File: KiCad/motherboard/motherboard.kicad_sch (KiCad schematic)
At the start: 489 parts, among them J1 Barrel_Jack_Switch, J11 Conn_01x06_Pin, J12 Conn_01x06_Pin, J13 Conn_01x04_Pin, J14 Conn_01x04_Pin, J15 Conn_01x04_Pin, J16 Conn_01x05_Socket, J17 DB25_Socket_MountingHoles, J18 Conn_01x09_Pin, J3 Conn_01x04_Pin, J4 Conn_01x05_Pin, Q1 NMOS, Q10 BSS138, Q2 NMOS, Q3 Q_NMOS_Depletion, Q4 Si2371EDS, Q5 BSS138, Q6 BSS138, Q7 BSS138, Q8 BSS138, Q9 BSS138, SW12 SW_Push, SW13 SW_Push, SW14 SW_Push, SW15 SW_Push, SW4 EmergencyStop, SW5 TiltSwitch, SW6 DoorSwitch, SW7 AdditionalSlot, U10 LTV-817S, U11 LTV-817S, U12 LTV-817S, U13 LTV-817S, U14 LTV-817S, U2 TMC2209, U3 TMC2209, U4 ASSR-1218, U5 24LC512, U6 P7805B-1000, U8 LTV-817S, U9 P7803B-1000

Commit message: schematics finished
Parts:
- removed C14, C15, C16, C17: 1u, symbol Device:C
- removed D2: GREEN_LED, symbol Device:LED
- removed D3: SM15T36CA, Diode_SMD:ST_D_SMC, symbol Diode:SM15T36CA
- removed J16: Conn_01x05_Socket, symbol Connector:Conn_01x05_Socket
- removed Q1, Q2: NMOS, symbol Simulation_SPICE:NMOS
- removed Q10, Q7, Q8, Q9: BSS138, Package_TO_SOT_SMD:SOT-23, symbol Transistor_FET:BSS138
- removed Q3: Q_NMOS_Depletion, symbol Device:Q_NMOS_Depletion
- removed Q4: Si2371EDS, Package_TO_SOT_SMD:SOT-23, symbol Transistor_FET:Si2371EDS
- removed R39, R44, R49, R54: 100R, symbol Device:R
- removed R40, R45, R48, R50, R53, R55, R58: 1k, symbol Device:R
- removed R46, R51, R56: 190R, symbol Device:R
- removed R47, R52, R57: 100k, symbol Device:R
- removed TP10, TP11, TP12, TP239, TP240, TP8, TP9: TestPoint, Connector_PinSocket_2.54mm:PinSocket_1x02_P2.54mm_Vertical, symbol Connector:TestPoint
- removed U12, U13, U14, U8: LTV-817S, Package_DIP:SMDIP-4_W9.53mm, symbol Isolator:LTV-817S
- added D2: SZSMF6L24CAT3G, Diode_SMD:D_SOD-123, symbol Device:D_TVS
- added D3: V8PAM103HM3H, Diode_SMD:Vishay_SMPA, symbol Device:D_Schottky
- added J2: Conn_01x02_Socket, TerminalBlock_Phoenix:TerminalBlock_Phoenix_MKDS-1,5-2_1x02_P5.00mm_Horizontal, symbol Connector:Conn_01x02_Socket
- added J5, J6: Conn_01x04_Pin, Connector_PinSocket_2.54mm:PinSocket_1x04_P2.54mm_Vertical, symbol Connector:Conn_01x04_Pin
- added J7, J8: 1761681-9, Connector_PinHeader_2.54mm:PinHeader_2x13_P2.54mm_Vertical, symbol Connector_Generic:Conn_02x13_Odd_Even
- added JP1: SolderJumper_2_Open, Jumper:SolderJumper-2_P1.3mm_Open_RoundedPad1.0x1.5mm, symbol Jumper:SolderJumper_2_Open
- added JP119: SolderJumper_2_Bridged, Resistor_SMD:R_0603_1608Metric, symbol Jumper:SolderJumper_2_Bridged
- added JP120: Jumper_2_Bridged, Connector_PinHeader_2.54mm:PinHeader_1x02_P2.54mm_Vertical, symbol Jumper:Jumper_2_Bridged
- added JP121: SolderJumper_2_Open, Resistor_SMD:R_0603_1608Metric, symbol Jumper:SolderJumper_2_Open
- added JP5: Jumper_2_Open, Connector_PinHeader_2.54mm:PinHeader_1x02_P2.54mm_Vertical, symbol Jumper:Jumper_2_Open
- added Q1, Q11, Q2, Q4: BSS138, Package_TO_SOT_SMD:SOT-23, symbol Transistor_FET:BSS138
- added Q3: SI2369DS-T1-GE3, Package_TO_SOT_SMD:TSOT-23, symbol Simulation_SPICE:PMOS
- added R33, R36: 100k, Resistor_SMD:R_0603_1608Metric, symbol Device:R
- added R34, R35: 1k, Resistor_SMD:R_0603_1608Metric, symbol Device:R
- added U7: ~, Package_SO:TSSOP-14_4.4x5mm_P0.65mm, symbol SymbolLib:LSF0204-Q1
- C1, C6, C7, C8, C9: footprint (none) -> Capacitor_SMD:C_0603_1608Metric
- C2, C3, C4, C5: footprint (none) -> Capacitor_SMD:C_1206_3216Metric
- D1, D10, D11, D4, D5, D6, D7, D8, D9: footprint (none) -> Diode_SMD:D_0603_1608Metric
- F1: value Fuse -> 576-0154007.DRTL; footprint (none) -> Fuse:Fuseholder_Littelfuse_Nano2_154x
- JP2, JP3, JP4: footprint (none) -> Jumper:SolderJumper-2_P1.3mm_Open_RoundedPad1.0x1.5mm
- R1, R14, R15, R16, R17, R18, R19, R2, R20, R21, R22, R23, R24, R25, R26, R27, R28, R29, R3, R30, R4: footprint (none) -> Resistor_SMD:R_0603_1608Metric
- R10: value R -> 27k; footprint (none) -> Resistor_SMD:R_0603_1608Metric
- R11, R12: value R -> 10k; footprint (none) -> Resistor_SMD:R_0603_1608Metric
- R13: value R -> 20k; footprint (none) -> Resistor_SMD:R_0603_1608Metric
- R31, R32: value R -> 4k7; footprint (none) -> Resistor_SMD:R_0603_1608Metric
- R41: value 190R -> 100R; footprint (none) -> Resistor_SMD:R_0603_1608Metric; now not fitted
- R42, R43: footprint (none) -> Resistor_SMD:R_0603_1608Metric; now not fitted
- R5, R8: value R -> 100R; footprint (none) -> Resistor_SMD:R_0603_1608Metric
- R6: value R -> 330R; footprint (none) -> Resistor_SMD:R_0603_1608Metric
- R7: value R -> 100k; footprint (none) -> Resistor_SMD:R_0603_1608Metric; now not fitted
- R9: value 500R -> 150R; footprint (none) -> Resistor_SMD:R_0603_1608Metric
- SW13, SW14, SW15: footprint (none) -> Connector_PinSocket_2.54mm:PinSocket_1x02_P2.54mm_Vertical
- SW4, SW5, SW6, SW7: footprint (none) -> TerminalBlock_Phoenix:TerminalBlock_Phoenix_MKDS-1,5-2_1x02_P5.00mm_Horizontal
- TP7: footprint Connector_PinSocket_2.54mm:PinSocket_1x02_P2.54mm_Vertical -> Connector_PinHeader_2.54mm:PinHeader_1x01_P2.54mm_Vertical
- U6, U9: footprint (none) -> Package_SIP:SIP3_11.6x8.5mm
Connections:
- net GND_SPI_LISTEN is gone; now on net GND: R42.1
- net +24V: now also D3.1 (K), Q3.3 (S)
- net +3V3: now also R43.2, R9.1, R36.1, U7.1 (VREF_A); no longer R8.1
- net +5V: no longer R41.2, U4.4
- net CLK_LISTEN: now also J5.4 (Pin_4), U7.5 (A4)
- net CLK_LISTEN_EXTERNAL: now also J6.4 (Pin_4), J7.4 (Pin_4), J8.4 (Pin_4), U7.10 (B4)
- net GND: now also R7.1, D2.1 (A1), J7.1 (Pin_1), J7.11 (Pin_11), J7.13 (Pin_13), J7.15 (Pin_15), J7.3 (Pin_3), J7.5 (Pin_5), J7.7 (Pin_7), J7.9 (Pin_9), J8.1 (Pin_1), J8.11 (Pin_11), J8.13 (Pin_13), J8.15 (Pin_15), J8.3 (Pin_3), J8.5 (Pin_5), J8.7 (Pin_7), J8.9 (Pin_9), JP1.2 (B), Q1.2 (S), Q11.2 (S), Q2.2 (S), Q4.2 (S), R33.1, U7.7 (GND); no longer U4.2
- net MISO_LISTEN: now also J5.3 (Pin_3), U7.4 (A3)
- net MISO_LISTEN_EXTERNAL: now also J6.3 (Pin_3), J7.6 (Pin_6), J8.6 (Pin_6), U7.11 (B3); no longer TP7.1
- net MOSI_LISTEN: now also J5.2 (Pin_2), U7.3 (A2)
- net MOSI_LISTEN_EXTERNAL: now also J6.2 (Pin_2), J7.8 (Pin_8), J8.8 (Pin_8), U7.12 (B2); no longer R43.2
- net MOT_ENN_DEBOUNCED: now also R41.1, R8.1, JP119.1 (A); no longer R7.1, R9.1
- net NSS_LISTEN: now also J5.1 (Pin_1), U7.2 (A1)
- net NSS_LISTEN_EXTERNAL: now also J6.1 (Pin_1), J7.10 (Pin_10), J8.10 (Pin_10), U7.13 (B1)
- net PDN_UART_MOT1: now also R34.1; no longer U2.3 (PDN/UART), U2.4 (PDN/UART)
- net PDN_UART_MOT2: now also R35.1; no longer U3.3 (PDN/UART), U3.4 (PDN/UART)
- net at R42.2: now also R41.2, Q4.1 (G); no longer R43.1
- net at R1.2, R2.2: now also Q11.1 (G)
- net at R8.2: now also Q1.1 (G), R33.2
- net at D1.1 (K): now also Q2.3 (D)
- net at SW7.1 (A): now also Q11.3 (D)
- net at D4.2 (A), D5.1 (K), F1.2: now also D2.2 (A2), D3.2 (A), Q3.1 (D)
- net at R7.2: now also R5.2, Q2.1 (G)
- net at R11.2, R12.1: now also Q3.2 (G)
- net ISOLATED_ENN_FEEDBACK: no longer names the net of U4.3
- net ISOLATED_ENN_FEEDBACK: now also J2.2 (Pin_2)
- new net: R35.2, U3.3 (PDN/UART), U3.4 (PDN/UART)
- new net: J7.23 (Pin_23), JP120.1 (A)
- new net: JP1.1 (A), R36.2, U7.8 (EN)
- new net: R34.2, U2.3 (PDN/UART), U2.4 (PDN/UART)
- new net: Q1.3 (D), U4.2
- new net: J2.1 (Pin_1), U4.4
- new net: J7.25 (Pin_25), JP5.1 (A)
- new net MOT_ENN: JP119.2 (B), JP121.1 (A)
- new net VCC_SPI: J8.23 (Pin_23), J8.25 (Pin_25), JP120.2 (B), JP5.2 (B), TP7.1, U7.14 (VREF_B)
- new net ~{MOT_ENN_DEBOUNCED}: JP121.2 (B), Q4.3 (D), R43.1
- no-connect marks 6 -> 24
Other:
- note added: "Csatlakozók"
- note added: "ESP32"
- note added: "Logikai szint illesztése"
- note added: "Negált jel lehetősege"
- note added: "Polaritásvédelem"
- note added: "Portok"
- note added: "R7: Amennyiben nem elegendő a vele párhuzamos út a spontán töltések elvezetésére"
- note added: "SPI IN"
- note added: "SPI OUT"
- note added: "Tápellátás"
- note added: "Túlfeszültségvédelem"
- note removed: "100R miért? Csak, h ne közvetlenül menjen?"
- note removed: "ESD"
- note removed: "Ez csak placeholder, meg kell beszélni a típusát még"
- note removed: "Ez nem tudom, jó választás-e. Azért ez van itt, mert ez már bennt volt a könyvtárnam, kétiránú és VRM = 30.8V"
- note removed: "Ez így miért nem jó, hogy nem 5V és 3v3 zener, hanem simán a 3v3-at kapcsolom"
- note removed: "Polarity indication"
- note removed: "Polarity indication?"
- note removed: "Pull downt azért raktam, mert le van választva -> nincs aktívan hajtva az alacsony szint Nem terheli ezn agyon a lehallgatottat? Milyen csati kellene?"
- note removed: "todo: footprintek kapcsolóknak csati, MOSFET-eket kell választani"
- moved on the sheet: C1, C18, C19, C20, C21, C8, C9, D1, D4, D5, F1, J1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

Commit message: PCB designs started
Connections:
- net BTN_FIX_AX: now also J18.3 (Pin_3), JP41.2 (B), TP96.1; no longer J18.2 (Pin_2), JP40.2 (B), TP95.1
- net BTN_MEMSLOT: now also J18.2 (Pin_2), JP40.2 (B), TP95.1; no longer J18.4 (Pin_4), JP42.2 (B), TP97.1
- net BTN_SET: now also J18.4 (Pin_4), JP42.2 (B), TP97.1; no longer J18.6 (Pin_6), JP44.2 (B), TP99.1
- net BTN_TRACKED_AX: now also J18.6 (Pin_6), JP44.2 (B), TP99.1; no longer J18.3 (Pin_3), JP41.2 (B), TP96.1

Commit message: main board pcb design started
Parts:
- TP100, TP101, TP102, TP103, TP104, TP105, TP106, TP107, TP108, TP109, TP110, TP111, TP112, TP113, TP114, TP115, TP116, TP117, TP118, TP119, TP120, TP121, TP122, TP123, TP124, TP125, TP126, TP127, TP128, TP129, TP13, TP130, TP131, TP132, TP133, TP134, TP135, TP136, TP137, TP138, TP139, TP14, TP140, TP141, TP142, TP143, TP144, TP145, TP146, TP147, TP148, TP149, TP15, TP150, TP151, TP152, TP153, TP154, TP155, TP156, TP157, TP158, TP159, TP16, TP160, TP161, TP162, TP163, TP164, TP165, TP166, TP167, TP168, TP169, TP17, TP170, TP171, TP172, TP173, TP174, TP175, TP176, TP177, TP178, TP179, TP18, TP180, TP181, TP182, TP183, TP184, TP185, TP186, TP187, TP188, TP189, TP19, TP190, TP191, TP192, TP193, TP194, TP195, TP196, TP197, TP198, TP199, TP20, TP200, TP201, TP202, TP203, TP204, TP205, TP206, TP207, TP208, TP209, TP21, TP210, TP211, TP212, TP213, TP214, TP215, TP216, TP217, TP218, TP219, TP22, TP220, TP221, TP222, TP223, TP224, TP225, TP226, TP227, TP228, TP229, TP23, TP230, TP231, TP232, TP233, TP234, TP235, TP236, TP237, TP238, TP24, TP241, TP242, TP25, TP26, TP27, TP28, TP29, TP30, TP31, TP32, TP33, TP34, TP35, TP36, TP37, TP38, TP39, TP40, TP41, TP42, TP43, TP44, TP45, TP46, TP47, TP48, TP49, TP50, TP51, TP52, TP53, TP54, TP55, TP56, TP57, TP58, TP59, TP60, TP61, TP62, TP63, TP64, TP65, TP66, TP67, TP68, TP69, TP70, TP71, TP72, TP73, TP74, TP75, TP76, TP77, TP78, TP79, TP80, TP81, TP82, TP83, TP84, TP85, TP86, TP87, TP88, TP89, TP90, TP91, TP92, TP93, TP94, TP95, TP96, TP97, TP98, TP99: footprint Connector_PinSocket_2.54mm:PinSocket_1x02_P2.54mm_Vertical -> Connector_PinSocket_2.54mm:PinSocket_1x01_P2.54mm_Vertical
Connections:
- net MOT_ENN: now also R5.1
- net MOT_ENN_DEBOUNCED: no longer R5.1
- net at U4.3: now also J2.1 (Pin_1); no longer J2.2 (Pin_2)
- net at U4.4: now also J2.2 (Pin_2); no longer J2.1 (Pin_1)
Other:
- note added: "Level shifter kikapcsolható J1 zárásával"
- moved on the sheet: J2

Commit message: main board pcb continued
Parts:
- added JP122, JP123, JP124, JP125, JP126, JP127, JP128, JP129, JP130, JP131, JP132, JP133, JP134, JP135, JP136, JP137, JP138, JP139, JP140, JP141, JP142, JP67, JP68, JP69, JP70, JP71, JP72: SolderJumper_2_Open, Resistor_SMD:R_0603_1608Metric_Pad0.98x0.95mm_HandSolder, symbol Jumper:SolderJumper_2_Open
- added TP131, TP132, TP133, TP134, TP135, TP136, TP185, TP186, TP187, TP188, TP189, TP190, TP240, TP241, TP242, TP243, TP244, TP245, TP246, TP247, TP248, TP249, TP250, TP251, TP252, TP253, TP254, TP255, TP256, TP257, TP258, TP259, TP260, TP262, TP263, TP264, TP265, TP266, TP267, TP268, TP269, TP270, TP271, TP272, TP273, TP274, TP275, TP276, TP277, TP278, TP279, TP280, TP281, TP282: TestPoint_Small, Connector_PinSocket_2.54mm:PinSocket_1x01_P2.54mm_Vertical, symbol Connector:TestPoint_Small
- renumbered C4 to C1, C20 to C10, C9 to C11, C7 to C12, C21 to C13, C1 to C3, C5 to C4, C3 to C5, C18 to C6, C6 to C7, C19 to C8, C8 to C9, D2 to D1, D11 to D10, D10 to D11, D4 to D2, D5 to D3, D3 to D4, D8 to D5, D7 to D6, D6 to D7, D1 to D8, J11 to J1, J15 to J10, J17 to J11, J5 to J12, J7 to J13, J6 to J14, J8 to J15, J1 to J2, J12 to J5, J13 to J6, J18 to J7, J2 to J8, J14 to J9, JP121 to JP1, JP13 to JP10, JP97 to JP100, JP98 to JP101, JP99 to JP102, JP100 to JP103, JP101 to JP104, JP54 to JP105, JP55 to JP106, JP56 to JP107, JP57 to JP108, JP58 to JP109, JP14 to JP11, JP59 to JP110, JP60 to JP111, JP61 to JP112, JP62 to JP113, JP63 to JP114, JP64 to JP115, JP65 to JP116, JP66 to JP117, JP67 to JP118, JP68 to JP119, JP15 to JP12, JP69 to JP120, JP118 to JP121, JP16 to JP13, JP17 to JP14, JP3 to JP143, JP5 to JP144, JP4 to JP145, JP120 to JP146, JP2 to JP147, JP1 to JP148, JP18 to JP15, JP19 to JP16, JP20 to JP17, JP21 to JP18, JP70 to JP19, JP119 to JP2, JP71 to JP20, JP72 to JP21, JP73 to JP22, JP74 to JP23, JP75 to JP24, JP76 to JP25, JP77 to JP26, JP78 to JP27, JP79 to JP28, JP80 to JP29, JP6 to JP3, JP81 to JP30, JP82 to JP31, JP83 to JP32, JP84 to JP33, JP85 to JP34, JP38 to JP35, JP39 to JP36, JP40 to JP37, JP41 to JP38, JP42 to JP39, JP7 to JP4, JP43 to JP40, JP44 to JP41, JP45 to JP42, JP46 to JP43, JP47 to JP44, JP48 to JP45, JP49 to JP46, JP50 to JP47, JP51 to JP48, JP52 to JP49, JP8 to JP5, JP53 to JP50, JP102 to JP51, JP103 to JP52, JP104 to JP53, JP105 to JP54, JP106 to JP55, JP107 to JP56, JP108 to JP57, JP109 to JP58, JP110 to JP59, JP9 to JP6, JP111 to JP60, JP112 to JP61, JP113 to JP62, JP114 to JP63, JP115 to JP64, JP116 to JP65, JP117 to JP66, JP10 to JP7, JP22 to JP73, JP23 to JP74, JP24 to JP75, JP25 to JP76, JP26 to JP77, JP27 to JP78, JP28 to JP79, JP11 to JP8, JP29 to JP80, JP30 to JP81, JP31 to JP82, JP32 to JP83, JP33 to JP84, JP34 to JP85, JP35 to JP86, JP36 to JP87, JP37 to JP88, JP86 to JP89, JP12 to JP9, JP87 to JP90, JP88 to JP91, JP89 to JP92, JP90 to JP93, JP91 to JP94, JP92 to JP95, JP93 to JP96, JP94 to JP97, JP95 to JP98, JP96 to JP99, Q11 to Q1, Q4 to Q2, Q1 to Q4, Q2 to Q5, Q5 to Q6, Q6 to Q7, R15 to R10, R14 to R11, R11 to R12, R8 to R14, R33 to R15, R5 to R16, R9 to R17, R7 to R18, R6 to R19, R34 to R20, R35 to R21, R31 to R22, R32 to R23, R16 to R24, R59 to R25, R60 to R26, R61 to R27, R62 to R28, R17 to R29, R41 to R3, R29 to R30, R18 to R31, R25 to R32, R19 to R33, R30 to R34, R24 to R35, R28 to R36, R63 to R37, R64 to R38, R22 to R39, R3 to R4, R23 to R40, R21 to R41, R26 to R42, R20 to R43, R27 to R44, R65 to R45, R66 to R46, R36 to R47, R42 to R5, R4 to R6, R43 to R7, R10 to R8, R12 to R9, SW4 to SW1, SW5 to SW2, SW6 to SW3, SW7 to SW4, SW12 to SW5, SW13 to SW6, SW14 to SW7, SW15 to SW8, TP15 to TP1, TP31 to TP10, TP96 to TP100, TP97 to TP101, TP98 to TP102, TP99 to TP103, TP100 to TP104, TP101 to TP105, TP102 to TP106, TP103 to TP107, TP104 to TP108, TP105 to TP109, TP33 to TP11, TP106 to TP110, TP107 to TP111, TP108 to TP112, TP221 to TP113, TP222 to TP114, TP223 to TP115, TP224 to TP116, TP225 to TP117, TP226 to TP118, TP227 to TP119, TP35 to TP12, TP228 to TP120, TP229 to TP121, TP230 to TP122, TP231 to TP123, TP232 to TP124, TP233 to TP125, TP234 to TP126, TP235 to TP127, TP236 to TP128, TP241 to TP129, TP37 to TP13, TP242 to TP130, TP45 to TP137, TP46 to TP138, TP47 to TP139, TP39 to TP14, TP48 to TP140, TP49 to TP141, TP50 to TP142, TP51 to TP143, TP52 to TP144, TP53 to TP145, TP54 to TP146, TP55 to TP147, TP56 to TP148, TP57 to TP149, TP41 to TP15, TP58 to TP150, TP59 to TP151, TP60 to TP152, TP173 to TP153, TP174 to TP154, TP175 to TP155, TP176 to TP156, TP177 to TP157, TP178 to TP158, TP179 to TP159, TP43 to TP16, TP180 to TP160, TP181 to TP161, TP182 to TP162, TP183 to TP163, TP184 to TP164, TP185 to TP165, TP186 to TP166, TP187 to TP167, TP188 to TP168, TP109 to TP169, TP141 to TP17, TP110 to TP170, TP111 to TP171, TP112 to TP172, TP113 to TP173, TP114 to TP174, TP115 to TP175, TP116 to TP176, TP117 to TP177, TP118 to TP178, TP119 to TP179, TP142 to TP18, TP120 to TP180, TP121 to TP181, TP122 to TP182, TP123 to TP183, TP124 to TP184, TP143 to TP19, TP61 to TP191, TP62 to TP192, TP63 to TP193, TP64 to TP194, TP65 to TP195, TP66 to TP196, TP67 to TP197, TP68 to TP198, TP69 to TP199, TP14 to TP2, TP144 to TP20, TP70 to TP200, TP71 to TP201, TP72 to TP202, TP73 to TP203, TP74 to TP204, TP75 to TP205, TP76 to TP206, TP189 to TP207, TP190 to TP208, TP191 to TP209, TP145 to TP21, TP192 to TP210, TP193 to TP211, TP194 to TP212, TP195 to TP213, TP196 to TP214, TP197 to TP215, TP198 to TP216, TP199 to TP217, TP200 to TP218, TP201 to TP219, TP146 to TP22, TP202 to TP220, TP203 to TP221, TP204 to TP222, TP125 to TP223, TP126 to TP224, TP127 to TP225, TP128 to TP226, TP129 to TP227, TP130 to TP228, TP131 to TP229, TP147 to TP23, TP132 to TP230, TP133 to TP231, TP134 to TP232, TP135 to TP233, TP136 to TP234, TP137 to TP235, TP138 to TP236, TP139 to TP237, TP140 to TP238, TP237 to TP239, TP148 to TP24, TP149 to TP25, TP150 to TP26, TP238 to TP261, TP151 to TP27, TP152 to TP28, TP6 to TP283, TP5 to TP284, TP4 to TP285, TP1 to TP286, TP7 to TP287, TP3 to TP288, TP2 to TP289, TP153 to TP29, TP17 to TP3, TP154 to TP30, TP155 to TP31, TP156 to TP32, TP77 to TP33, TP78 to TP34, TP79 to TP35, TP80 to TP36, TP81 to TP37, TP82 to TP38, TP83 to TP39, TP19 to TP4, TP84 to TP40, TP85 to TP41, TP86 to TP42, TP87 to TP43, TP88 to TP44, TP89 to TP45, TP90 to TP46, TP91 to TP47, TP92 to TP48, TP205 to TP49, TP21 to TP5, TP206 to TP50, TP207 to TP51, TP208 to TP52, TP209 to TP53, TP210 to TP54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
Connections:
- net GND: now also JP131.2 (B), JP132.2 (B), JP133.2 (B), JP134.2 (B), JP135.2 (B), JP136.2 (B), JP137.2 (B), JP138.2 (B), JP139.2 (B), JP140.2 (B), JP141.2 (B), JP142.2 (B), TP271.1, TP272.1, TP273.1, TP274.1, TP275.1, TP276.1, TP277.1, TP278.1, TP279.1, TP280.1, TP281.1, TP282.1; no longer U3.11-19 (GND), U3.11-20 (GND), U3.11-22 (GND), U3.11-49 (GND), U3.11-60 (GND), U3.11-8 (GND), U3.12-20 (GND), U3.12-32 (AGND), U3.12-39 (GND), U3.12-54 (GND), U3.12-63 (GND), U3.12-9 (GND)
- net at U3.11-12 (IOREF): now also JP126.1 (A), TP244.1
- net at U3.11-14 (RESET): now also JP130.1 (A), TP248.1
- net at U3.11-16 (3V3): now also JP125.1 (A), TP243.1
- net at U3.11-18 (5V): now also JP124.1 (A), TP242.1
- net at U3.11-24 (VIN): now also JP123.1 (A), TP241.1
- net at U3.11-33 (VBAT): now also JP122.1 (A), TP240.1
- net at U3.11-5 (VDD): now also JP127.1 (A), TP245.1
- net at U3.12-7 (AVDD): now also JP129.1 (A), TP247.1
- net at U3.12-8 (U5V): now also JP128.1 (A), TP246.1
- net at U3.11-10 (NC): now also JP72.1 (A), TP136.1
- net at U3.11-26 (NC): now also JP71.1 (A), TP135.1
- net at U3.11-29 (PH0): now also JP67.1 (A), TP131.1
- net at U3.11-31 (PH1): now also JP68.1 (A), TP132.1
- net at U3.11-67 (NC): now also JP70.1 (A), TP134.1
- net at U3.11-7 (BOOT0): now also JP69.1 (A), TP133.1
- new net: JP124.2 (B), TP264.1
- new net: JP132.1 (A), TP250.1, U3.11-19 (GND)
- new net: JP133.1 (A), TP251.1, U3.11-20 (GND)
- new net: JP134.1 (A), TP252.1, U3.11-22 (GND)
- new net: JP139.1 (A), TP257.1, U3.11-49 (GND)
- new net: JP141.1 (A), TP259.1, U3.11-60 (GND)
- new net: JP140.1 (A), TP258.1, U3.11-8 (GND)
- new net: JP135.1 (A), TP253.1, U3.12-20 (GND)
- new net: JP131.1 (A), TP249.1, U3.12-32 (AGND)
- new net: JP136.1 (A), TP254.1, U3.12-39 (GND)
- new net: JP137.1 (A), TP255.1, U3.12-54 (GND)
- new net: JP138.1 (A), TP256.1, U3.12-63 (GND)
- new net: JP142.1 (A), TP260.1, U3.12-9 (GND)
- new net: JP72.2 (B), TP190.1
- new net: JP68.2 (B), TP186.1
- new net: JP67.2 (B), TP185.1
- new net: JP69.2 (B), TP187.1
- new net: JP130.2 (B), TP270.1
- new net: JP122.2 (B), TP262.1
- new net: JP127.2 (B), TP267.1
- new net: JP126.2 (B), TP266.1
- new net: JP128.2 (B), TP268.1
- new net: JP70.2 (B), TP188.1
- new net: JP123.2 (B), TP263.1
- new net: JP71.2 (B), TP189.1
- new net: JP129.2 (B), TP269.1
- new net: JP125.2 (B), TP265.1
- no-connect marks 24 -> 33

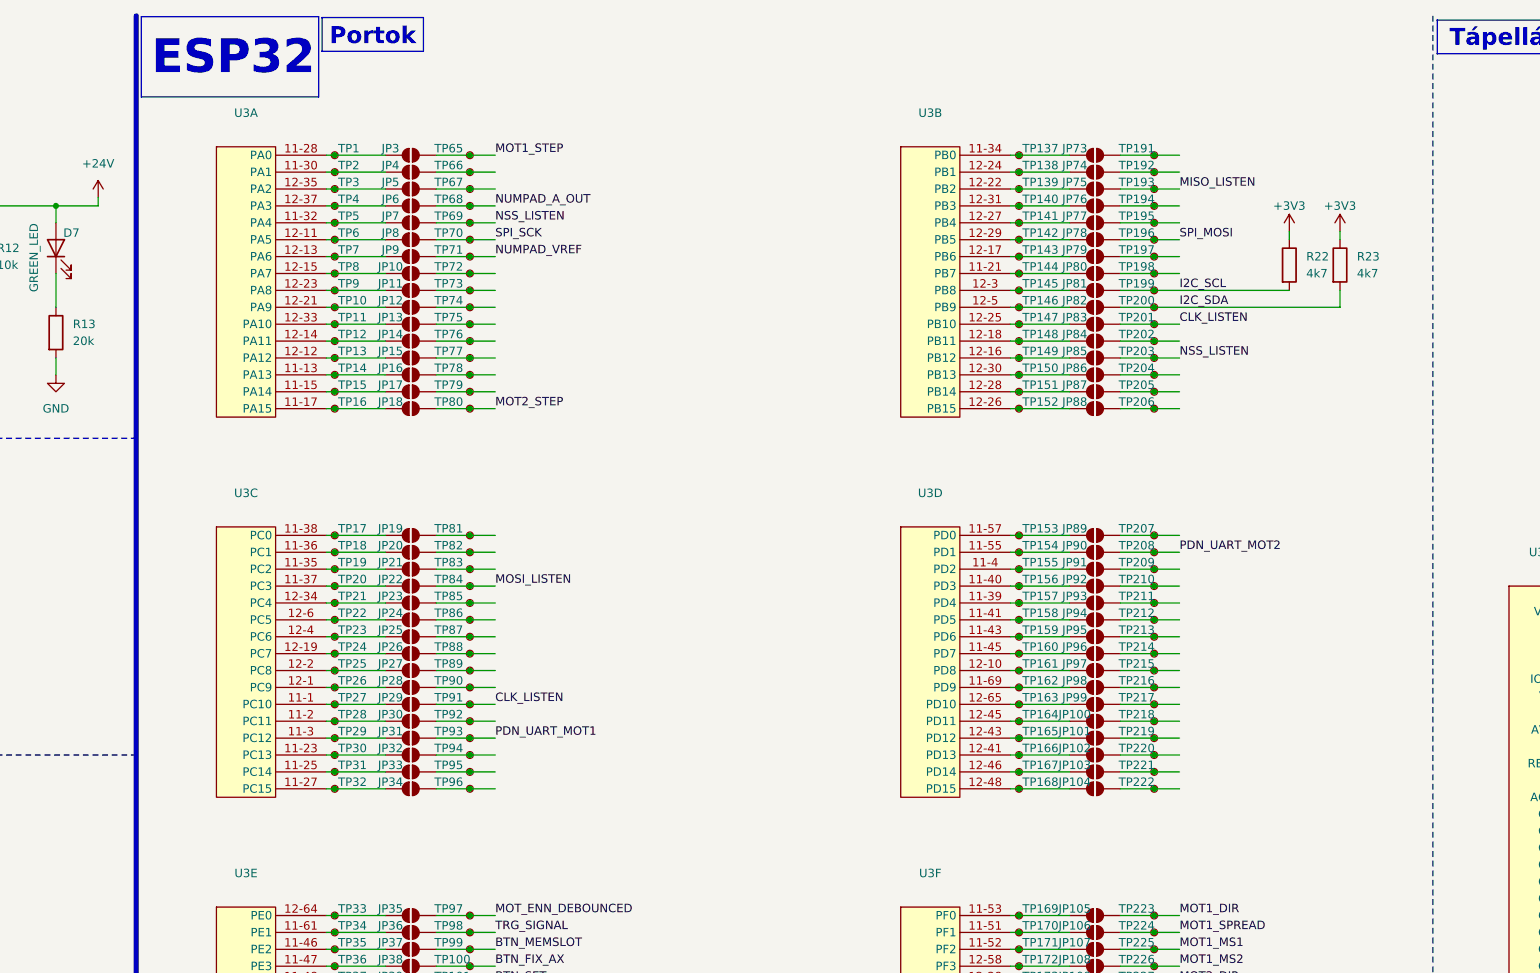
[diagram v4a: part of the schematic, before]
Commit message: motherboard pcb layout (MCU)
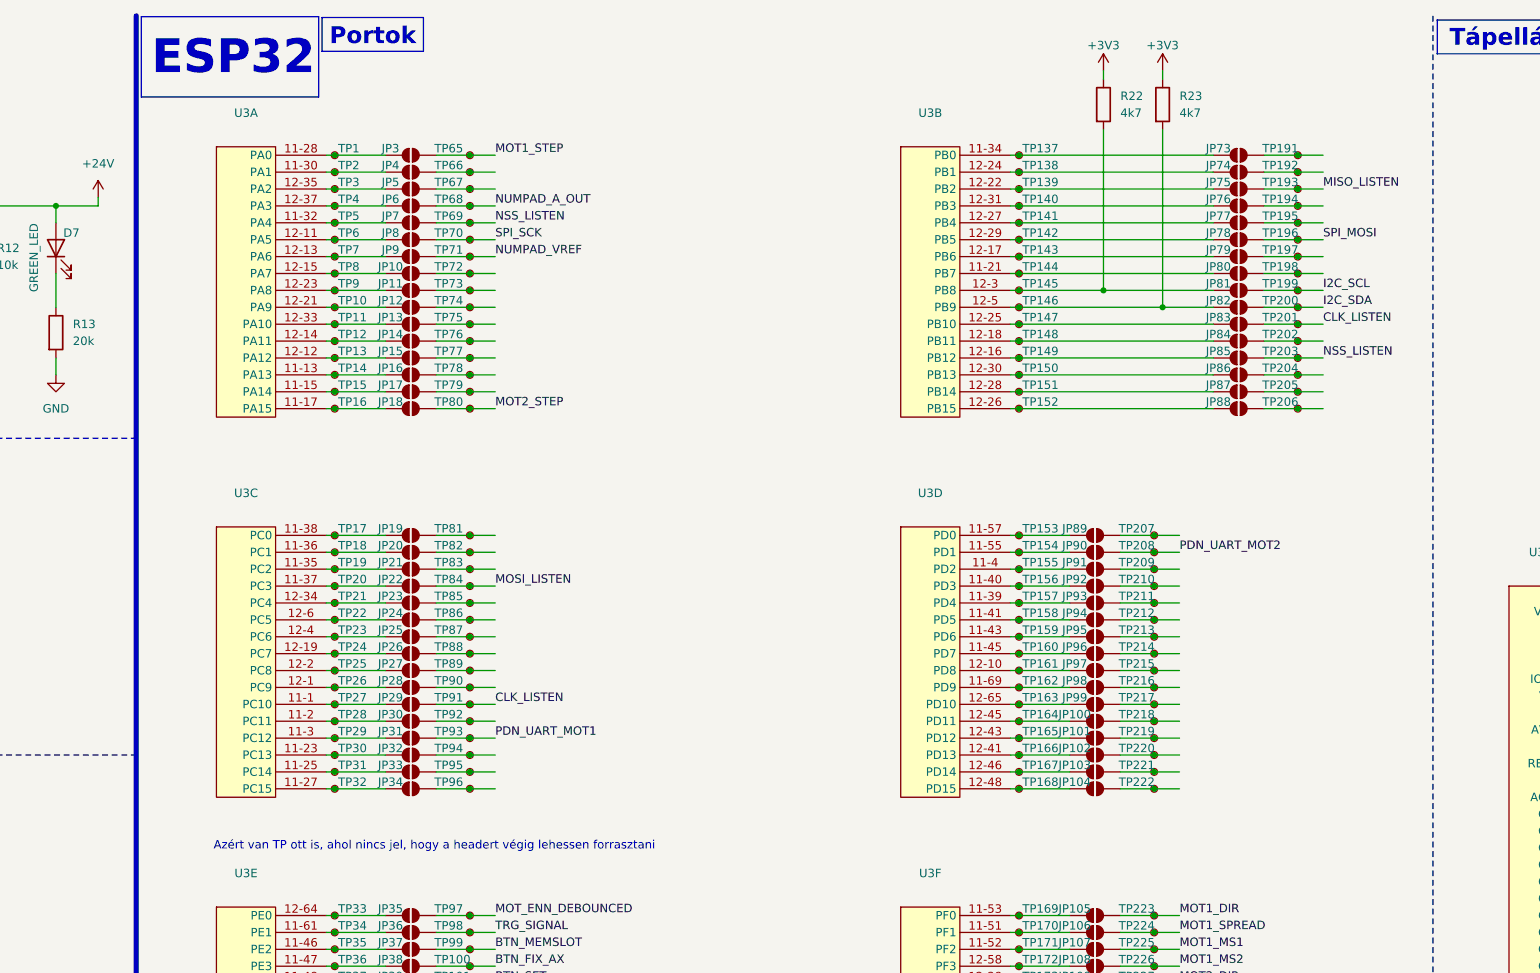
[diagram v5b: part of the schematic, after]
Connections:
- net I2C_SCL: no longer R22.2
- net I2C_SDA: no longer R23.2
- net at JP82.1 (A), TP146.1, U3.12-5 (PB9): now also R23.2
- net at JP81.1 (A), TP145.1, U3.12-3 (PB8): now also R22.2
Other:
- note added: "Azért van TP ott is, ahol nincs jel, hogy a headert végig lehessen forrasztani"
- moved on the sheet: JP73, JP74, JP75, JP76, JP77, JP78, JP79, JP80, JP81, JP82, JP83, JP84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

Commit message: motherboard PCB design
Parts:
- added TP1: TestPoint, TestPoint:TestPoint_Pad_D2.0mm, symbol Connector:TestPoint
- JP1: now not fitted
- SW5, SW6, SW7, SW8: footprint Connector_PinSocket_2.54mm:PinSocket_1x02_P2.54mm_Vertical -> Connector_JST:JST_PH_B2B-PH-K_1x02_P2.00mm_Vertical
- renumbered JP116 to JP100, JP117 to JP101, JP118 to JP102, JP119 to JP103, JP120 to JP104, JP73 to JP105, JP74 to JP106, JP75 to JP107, JP76 to JP108, JP77 to JP109, JP78 to JP110, JP79 to JP111, JP80 to JP112, JP81 to JP113, JP82 to JP114, JP83 to JP115, JP84 to JP116, JP85 to JP117, JP86 to JP118, JP87 to JP119, JP88 to JP120, JP89 to JP73, JP90 to JP74, JP91 to JP75, JP92 to JP76, JP93 to JP77, JP94 to JP78, JP95 to JP79, JP96 to JP80, JP97 to JP81, JP98 to JP82, JP99 to JP83, JP100 to JP84, JP101 to JP85, JP102 to JP86, JP103 to JP87, JP104 to JP88, JP105 to JP89, JP106 to JP90, JP107 to JP91, JP108 to JP92, JP109 to JP93, JP110 to JP94, JP111 to JP95, JP112 to JP96, JP113 to JP97, JP114 to JP98, JP115 to JP99, TP9 to TP10, TP99 to TP100, TP100 to TP101, TP101 to TP102, TP102 to TP103, TP103 to TP104, TP104 to TP105, TP105 to TP106, TP106 to TP107, TP107 to TP108, TP108 to TP109, TP10 to TP11, TP109 to TP110, TP110 to TP111, TP111 to TP112, TP112 to TP113, TP113 to TP114, TP114 to TP115, TP115 to TP116, TP116 to TP117, TP117 to TP118, TP118 to TP119, TP11 to TP12, TP119 to TP120, TP120 to TP121, TP121 to TP122, TP122 to TP123, TP123 to TP124, TP124 to TP125, TP125 to TP126, TP126 to TP127, TP127 to TP128, TP128 to TP129, TP12 to TP13, TP129 to TP130, TP130 to TP131, TP131 to TP132, TP132 to TP133, TP133 to TP134, TP134 to TP135, TP135 to TP136, TP136 to TP137, TP137 to TP138, TP138 to TP139, TP13 to TP14, TP139 to TP140, TP140 to TP141, TP141 to TP142, TP142 to TP143, TP143 to TP144, TP144 to TP145, TP145 to TP146, TP146 to TP147, TP147 to TP148, TP148 to TP149, TP14 to TP15, TP149 to TP150, TP150 to TP151, TP151 to TP152, TP152 to TP153, TP153 to TP154, TP154 to TP155, TP155 to TP156, TP156 to TP157, TP157 to TP158, TP158 to TP159, TP15 to TP16, TP159 to TP160, TP160 to TP161, TP161 to TP162, TP162 to TP163, TP163 to TP164, TP164 to TP165, TP165 to TP166, TP166 to TP167, TP167 to TP168, TP168 to TP169, TP16 to TP17, TP169 to TP170, TP170 to TP171, TP171 to TP172, TP172 to TP173, TP173 to TP174, TP174 to TP175, TP175 to TP176, TP176 to TP177, TP177 to TP178, TP178 to TP179, TP17 to TP18, TP179 to TP180, TP180 to TP181, TP181 to TP182, TP182 to TP183, TP183 to TP184, TP184 to TP185, TP185 to TP186, TP186 to TP187, TP187 to TP188, TP188 to TP189, TP18 to TP19, TP189 to TP190, TP190 to TP191, TP207 to TP192, TP208 to TP193, TP209 to TP194, TP210 to TP195, TP211 to TP196, TP212 to TP197, TP213 to TP198, TP214 to TP199, TP1 to TP2, TP19 to TP20, TP215 to TP200, TP216 to TP201, TP217 to TP202, TP218 to TP203, TP219 to TP204, TP220 to TP205, TP221 to TP206, TP222 to TP207, TP223 to TP208, TP224 to TP209, TP20 to TP21, TP225 to TP210, TP226 to TP211, TP227 to TP212, TP228 to TP213, TP229 to TP214, TP230 to TP215, TP231 to TP216, TP232 to TP217, TP233 to TP218, TP234 to TP219, TP21 to TP22, TP235 to TP220, TP236 to TP221, TP237 to TP222, TP238 to TP223, TP191 to TP224, TP192 to TP225, TP193 to TP226, TP194 to TP227, TP195 to TP228, TP196 to TP229, TP22 to TP23, TP197 to TP230, TP198 to TP231, TP199 to TP232, TP200 to TP233, TP201 to TP234, TP202 to TP235, TP203 to TP236, TP204 to TP237, TP205 to TP238, TP206 to TP239, TP23 to TP24, TP239 to TP240, TP240 to TP241, TP241 to TP242, TP242 to TP243, TP243 to TP244, TP244 to TP245, TP245 to TP246, TP246 to TP247, TP247 to TP248, TP248 to TP249, TP24 to TP25, TP249 to TP250, TP250 to TP251, TP251 to TP252, TP252 to TP253, TP253 to TP254, TP254 to TP255, TP255 to TP256, TP256 to TP257, TP257 to TP258, TP258 to TP259, TP25 to TP26, TP259 to TP260, TP260 to TP261, TP261 to TP262, TP262 to TP263, TP263 to TP264, TP264 to TP265, TP265 to TP266, TP266 to TP267, TP267 to TP268, TP268 to TP269, TP26 to TP27, TP269 to TP270, TP270 to TP271, TP271 to TP272, TP272 to TP273, TP273 to TP274, TP274 to TP275, TP275 to TP276, TP276 to TP277, TP277 to TP278, TP278 to TP279, TP27 to TP28, TP279 to TP280, TP280 to TP281, TP281 to TP282, TP282 to TP283, TP283 to TP284, TP284 to TP285, TP285 to TP286, TP286 to TP287, TP287 to TP288, TP288 to TP289, TP28 to TP29, TP289 to TP290, TP2 to TP3, TP29 to TP30, TP30 to TP31, TP31 to TP32, TP32 to TP33, TP33 to TP34, TP34 to TP35, TP35 to TP36, TP36 to TP37, TP37 to TP38, TP38 to TP39, TP3 to TP4, TP39 to TP40, TP40 to TP41, TP41 to TP42, TP42 to TP43, TP43 to TP44, TP44 to TP45, TP45 to TP46, TP46 to TP47, TP47 to TP48, TP48 to TP49, TP4 to TP5, TP49 to TP50, TP50 to TP51, TP51 to TP52, TP52 to TP53, TP53 to TP54, TP54 to TP55, TP55 to TP56, TP56 to TP57, TP57 to TP58, TP58 to TP59, TP5 to TP6, TP59 to TP60, TP60 to TP61, TP61 to TP62, TP62 to TP63, TP63 to TP64, TP64 to TP65, TP65 to TP66, TP66 to TP67, TP67 to TP68, TP68 to TP69, TP6 to TP7, TP69 to TP70, TP70 to TP71, TP71 to TP72, TP72 to TP73, TP73 to TP74, TP74 to TP75, TP75 to TP76, TP76 to TP77, TP77 to TP78, TP78 to TP79, TP7 to TP8, TP79 to TP80, TP80 to TP81, TP81 to TP82, TP82 to TP83, TP83 to TP84, TP84 to TP85, TP85 to TP86, TP86 to TP87, TP87 to TP88, TP88 to TP89, TP8 to TP9, TP89 to TP90, TP90 to TP91, TP91 to TP92, TP92 to TP93, TP93 to TP94, TP94 to TP95, TP95 to TP96, TP96 to TP97, TP97 to TP98, TP98 to TP99
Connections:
- net +3V3: now also C12.1, R40.2
- net +5V: no longer C12.1, R40.2
- net MOT_ENN: now also U5.8 (EN), U6.8 (EN), TP1.1
- net MOT_ENN_DEBOUNCED: no longer U5.8 (EN), U6.8 (EN)
- net TRG_RB_OUT: now also JP21.2 (B), TP84.1; no longer JP101.2 (B), TP220.1
- new net: JP101.2 (B), TP220.1
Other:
- moved on the sheet: J13, J15, JP144, JP146, TP288

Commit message: motherboard PCCB done, review needed
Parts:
- added H1, H2, H3, H4, H5, H6, H7, H8: MountingHole, MountingHole:MountingHole_3.2mm_M3, symbol Mechanical:MountingHole
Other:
- note added: "Rögzítőfuratok"
